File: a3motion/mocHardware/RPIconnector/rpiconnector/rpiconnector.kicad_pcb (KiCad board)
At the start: 2 copper layers, 56 x 21.9 mm, 11 parts, among them J1 Conn_01x05_Male, J2 Conn_02x05_Odd_Even, Q1 BSS138, Q2 BSS138, U1 USB-C

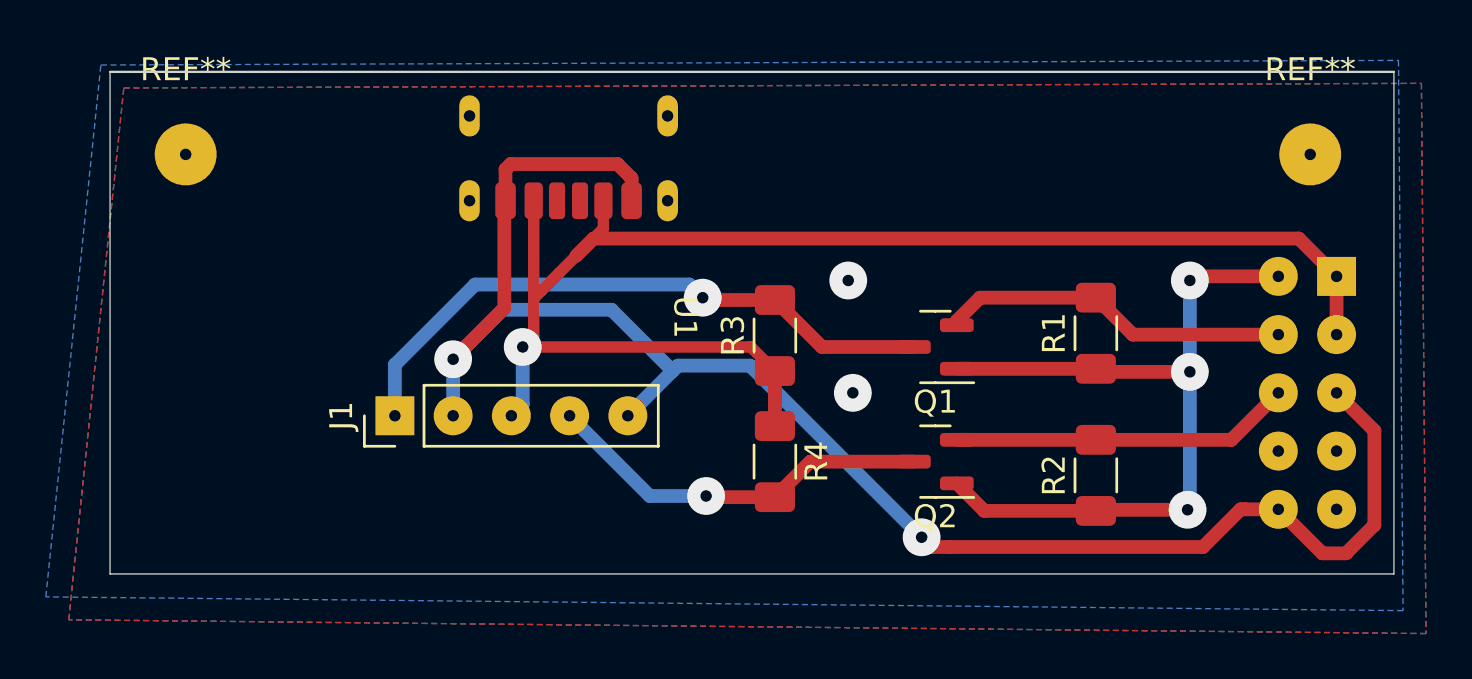
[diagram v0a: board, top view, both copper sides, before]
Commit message: cleaned libs and finished main und rpi pcb
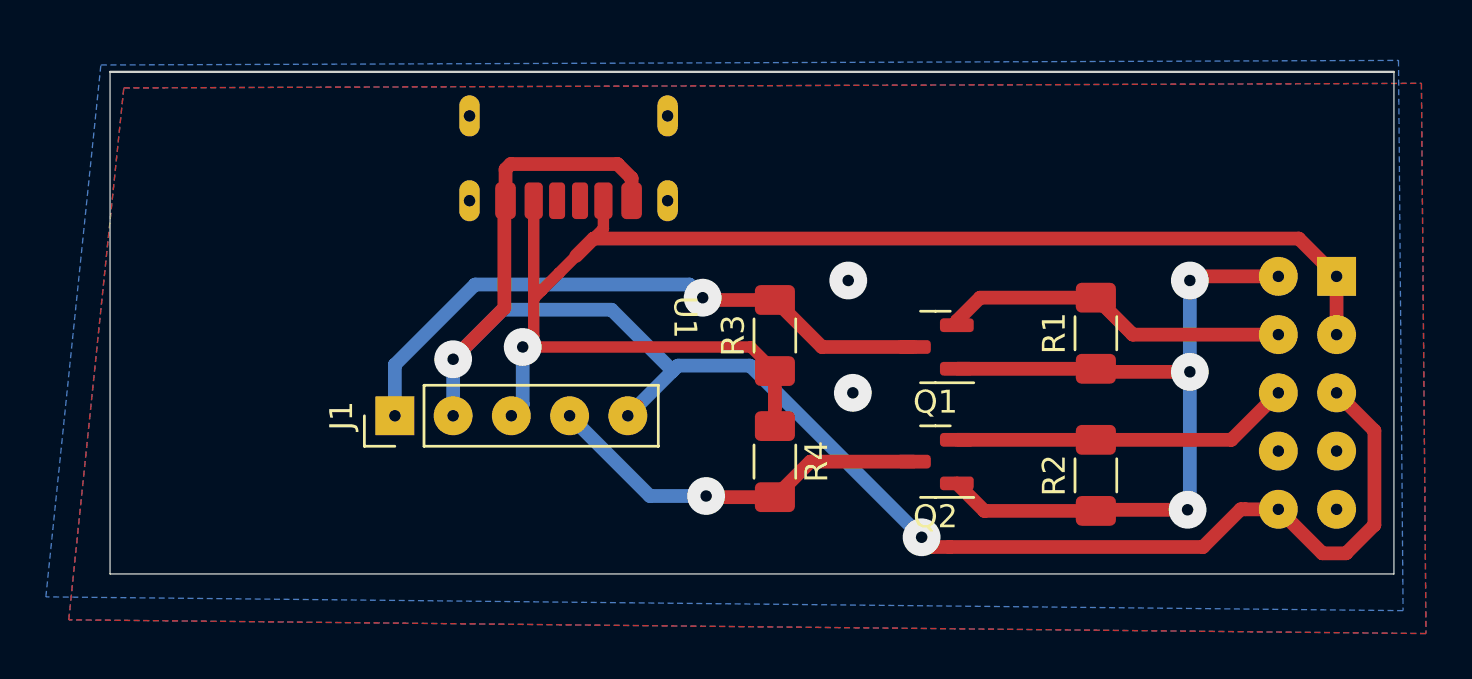
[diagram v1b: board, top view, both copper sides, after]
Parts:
- removed REF** (x2): MountingHole_2.7mm, MountingHole:MountingHole_2.7mm
- U1: footprint .Ambisonic:USB-C -> 3dAudioFoot:USB-C
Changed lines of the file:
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@@
   (net 11 "GPIO14")
   (net 12 "GPIO15")
-  (footprint "MountingHole:MountingHole_2.7mm" (layer "F.Cu")
-    (at 120.3 56.1)
-    (descr "Mounting Hole 2.7mm, no annular")
-    (tags "mounting hole 2.7mm no annular")
-    (attr exclude_from_pos_files exclude_from_bom)
-    (fp_text reference "REF**" (at 0 -3.7) (layer "F.SilkS")
-      (effects (font (size 1 1) (thickness 0.15)))
-    )
-    (fp_text value "MountingHole_2.7mm" (at 0 3.7) (layer "F.Fab")
-      (effects (font (size 1 1) (thickness 0.15)))
-    )
-    (fp_text user "${REFERENCE}" (at 0.3 0) (layer "F.Fab")
-      (effects (font (size 1 1) (thickness 0.15)))
-    )
-    (fp_circle (center 0 0) (end 2.7 0) (layer "Cmts.User") (width 0.15) (fill none))
-    (fp_circle (center 0 0) (end 2.95 0) (layer "F.CrtYd") (width 0.05) (fill none))
-    (pad "" np_thru_hole circle locked (at 0 0) (size 2.7 2.7) (drill 0.5) (layers *.Cu *.Mask))
-  )
   (footprint "Package_TO_SOT_SMD:SOT-23" (layer "F.Cu")
     (at 153 64.5 180)
@@
       (rotate (xyz 0 0 0))
     )
-  )
-  (footprint "MountingHole:MountingHole_2.7mm" (layer "F.Cu")
-    (at 169.35 56.1)
-    (descr "Mounting Hole 2.7mm, no annular")
-    (tags "mounting hole 2.7mm no annular")
-    (attr exclude_from_pos_files exclude_from_bom)
-    (fp_text reference "REF**" (at 0 -3.7) (layer "F.SilkS")
-      (effects (font (size 1 1) (thickness 0.15)))
-    )
-    (fp_text value "MountingHole_2.7mm" (at 0 3.7) (layer "F.Fab")
-      (effects (font (size 1 1) (thickness 0.15)))
-    )
-    (fp_text user "${REFERENCE}" (at 0.3 0) (layer "F.Fab")
-      (effects (font (size 1 1) (thickness 0.15)))
-    )
-    (fp_circle (center 0 0) (end 2.7 0) (layer "Cmts.User") (width 0.15) (fill none))
-    (fp_circle (center 0 0) (end 2.95 0) (layer "F.CrtYd") (width 0.05) (fill none))
-    (pad "" np_thru_hole circle locked (at 0 0) (size 2.7 2.7) (drill 0.5) (layers *.Cu *.Mask))
   )
   (footprint "Connector_PinHeader_2.54mm:PinHeader_1x05_P2.54mm_Vertical" (layer "F.Cu")
@@
       (rotate (xyz 0 0 0))
     )
+  )
+  (footprint "3dAudioFoot:USB-C" (layer "F.Cu")
+    (at 137 50.5 180)
+    (property "Sheetfile" "rpiconnector.kicad_sch")
+    (property "Sheetname" "")
+    (attr smd)
+    (fp_text reference "U1" (at -5.08 -12.7 270 unlocked) (layer "F.SilkS")
+      (effects (font (size 1 1) (thickness 0.15)))
+    )
+    (fp_text value "USB-C" (at 5.08 -10.16 180 unlocked) (layer "F.Fab")
+      (effects (font (size 1 1) (thickness 0.15)))
+    )
+    (fp_rect (start -4.572 -8.128) (end 4.572 -1.016) (layer "Dwgs.User") (width 0.12) (fill none))
+    (pad "" np_thru_hole oval (at 4.32 -3.92 180) (size 0.9 1.8) (drill 0.5) (layers F&B.Cu *.Mask))
+    (pad "" np_thru_hole oval (at -4.32 -3.92 180) (size 0.9 1.8) (drill 0.5) (layers F&B.Cu *.Mask))
+    (pad "" np_thru_hole oval (at -4.32 -7.62 180) (size 0.9 1.8) (drill 0.5) (layers F&B.Cu *.Mask))
+    (pad "" np_thru_hole oval (at 4.32 -7.62 180) (size 0.9 1.8) (drill 0.5) (layers F&B.Cu *.Mask))
+    (pad "1" smd roundrect (at -2.75 -7.622136 180) (size 0.9 1.6) (layers "F.Cu" "F.Paste" "F.Mask") (roundrect_rratio 0.25)
+      (net 2 "GND") (pinfunction "GND") (pintype "power_out"))
+    (pad "2" smd roundrect (at -1.52 -7.62 180) (size 0.8 1.6) (layers "F.Cu" "F.Paste" "F.Mask") (roundrect_rratio 0.25)
+      (net 3 "5v") (pinfunction "VBUS") (pintype "power_out"))
+    (pad "3" smd roundrect (at -0.5 -7.62 180) (size 0.7 1.6) (layers "F.Cu" "F.Paste" "F.Mask") (roundrect_rratio 0.25)
+      (net 8 "unconnected-(U1-Pad3)") (pinfunction "CC1") (pintype "input+no_connect"))
+    (pad "4" smd roundrect (at 0.5 -7.62 180) (size 0.7 1.6) (layers "F.Cu" "F.Paste" "F.Mask") (roundrect_rratio 0.25)
+      (net 9 "unconnected-(U1-Pad4)") (pinfunction "CC2") (pintype "input+no_connect"))
+    (pad "5" smd roundrect (at 1.52 -7.62 180) (size 0.8 1.6) (layers "F.Cu" "F.Paste" "F.Mask") (roundrect_rratio 0.25)
+      (net 3 "5v") (pinfunction "VBUS") (pintype "power_out"))
+    (pad "6" smd roundrect (at 2.75 -7.62 180) (size 0.9 1.6) (layers "F.Cu" "F.Paste" "F.Mask") (roundrect_rratio 0.25)
+      (net 2 "GND") (pinfunction "GND") (pintype "power_out"))
   )
   (footprint "Resistor_SMD:R_1206_3216Metric_Pad1.30x1.75mm_HandSolder" (layer "F.Cu")
@@
     )
   )
-  (footprint ".Ambisonic:USB-C" (layer "F.Cu")
-    (at 137 50.5 180)
-    (property "Sheetfile" "rpiconnector.kicad_sch")
-    (property "Sheetname" "")
-    (attr smd)
-    (fp_text reference "U1" (at -5.08 -12.7 270 unlocked) (layer "F.SilkS")
-      (effects (font (size 1 1) (thickness 0.15)))
-    )
-    (fp_text value "USB-C" (at 5.08 -10.16 180 unlocked) (layer "F.Fab")
-      (effects (font (size 1 1) (thickness 0.15)))
-    )
-    (fp_rect (start -4.572 -8.128) (end 4.572 -1.016) (layer "Dwgs.User") (width 0.12) (fill none))
-    (pad "" np_thru_hole oval (at 4.32 -3.92 180) (size 0.9 1.8) (drill 0.5) (layers F&B.Cu *.Mask))
-    (pad "" np_thru_hole oval (at 4.32 -7.62 180) (size 0.9 1.8) (drill 0.5) (layers F&B.Cu *.Mask))
-    (pad "" np_thru_hole oval (at -4.32 -3.92 180) (size 0.9 1.8) (drill 0.5) (layers F&B.Cu *.Mask))
-    (pad "" np_thru_hole oval (at -4.32 -7.62 180) (size 0.9 1.8) (drill 0.5) (layers F&B.Cu *.Mask))
-    (pad "1" smd roundrect (at -2.75 -7.622136 180) (size 0.9 1.6) (layers "F.Cu" "F.Paste" "F.Mask") (roundrect_rratio 0.25)
-      (net 2 "GND") (pinfunction "GND") (pintype "power_out"))
-    (pad "2" smd roundrect (at -1.52 -7.62 180) (size 0.8 1.6) (layers "F.Cu" "F.Paste" "F.Mask") (roundrect_rratio 0.25)
-      (net 3 "5v") (pinfunction "VBUS") (pintype "power_out"))
-    (pad "3" smd roundrect (at -0.5 -7.62 180) (size 0.7 1.6) (layers "F.Cu" "F.Paste" "F.Mask") (roundrect_rratio 0.25)
-      (net 8 "unconnected-(U1-Pad3)") (pinfunction "CC1") (pintype "input+no_connect"))
-    (pad "4" smd roundrect (at 0.5 -7.62 180) (size 0.7 1.6) (layers "F.Cu" "F.Paste" "F.Mask") (roundrect_rratio 0.25)
-      (net 9 "unconnected-(U1-Pad4)") (pinfunction "CC2") (pintype "input+no_connect"))
-    (pad "5" smd roundrect (at 1.52 -7.62 180) (size 0.8 1.6) (layers "F.Cu" "F.Paste" "F.Mask") (roundrect_rratio 0.25)
-      (net 3 "5v") (pinfunction "VBUS") (pintype "power_out"))
-    (pad "6" smd roundrect (at 2.75 -7.62 180) (size 0.9 1.6) (layers "F.Cu" "F.Paste" "F.Mask") (roundrect_rratio 0.25)
-      (net 2 "GND") (pinfunction "GND") (pintype "power_out"))
-  )
   (footprint "Resistor_SMD:R_1206_3216Metric_Pad1.30x1.75mm_HandSolder" (layer "F.Cu")
